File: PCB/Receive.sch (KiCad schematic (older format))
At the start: 9 parts

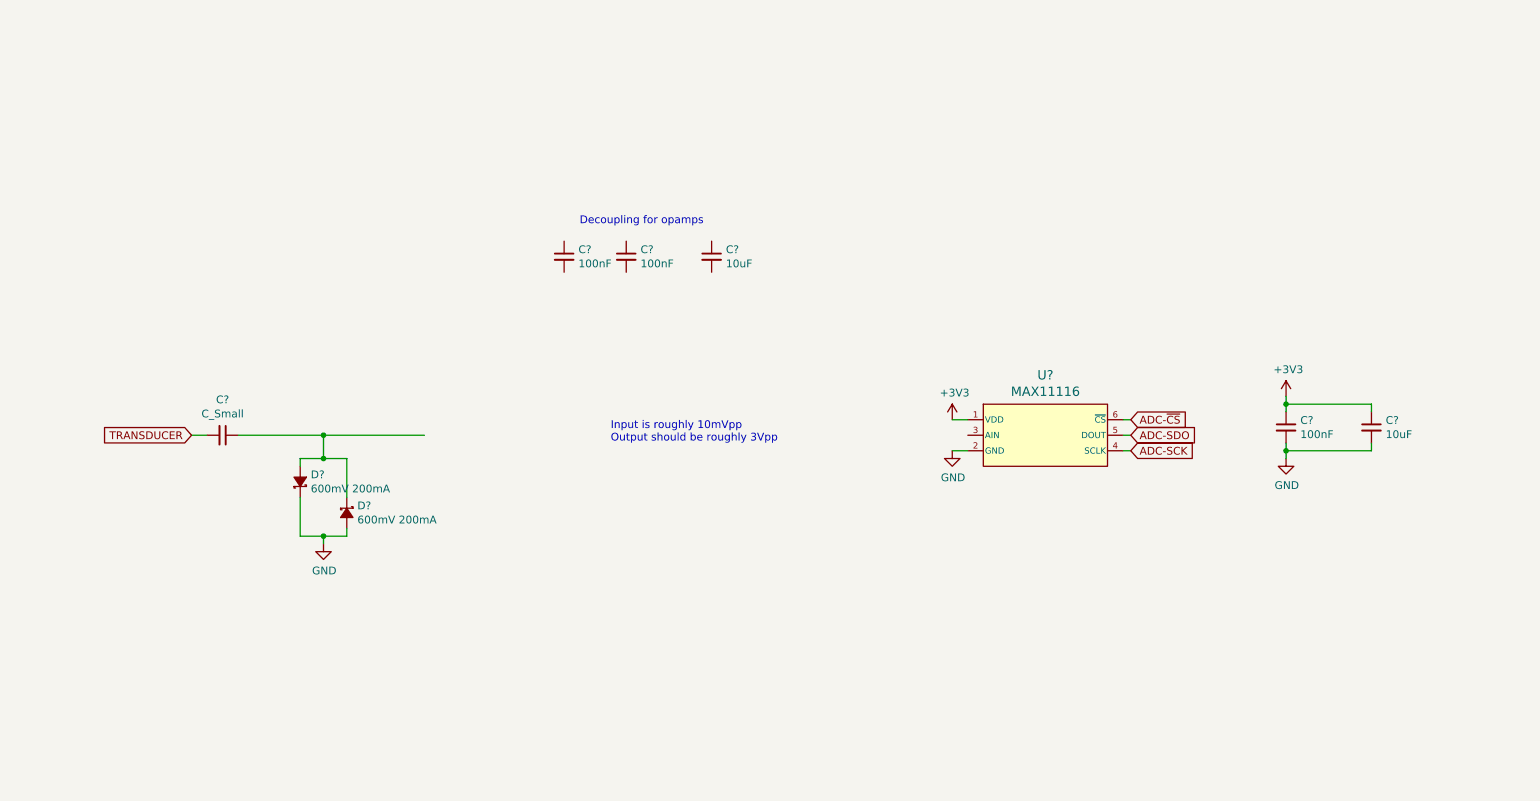
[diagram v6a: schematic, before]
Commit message: Added receive amplification circuit, added opamps for receive to library, added digital potentiometer to library, connected VGA stages to FPGA
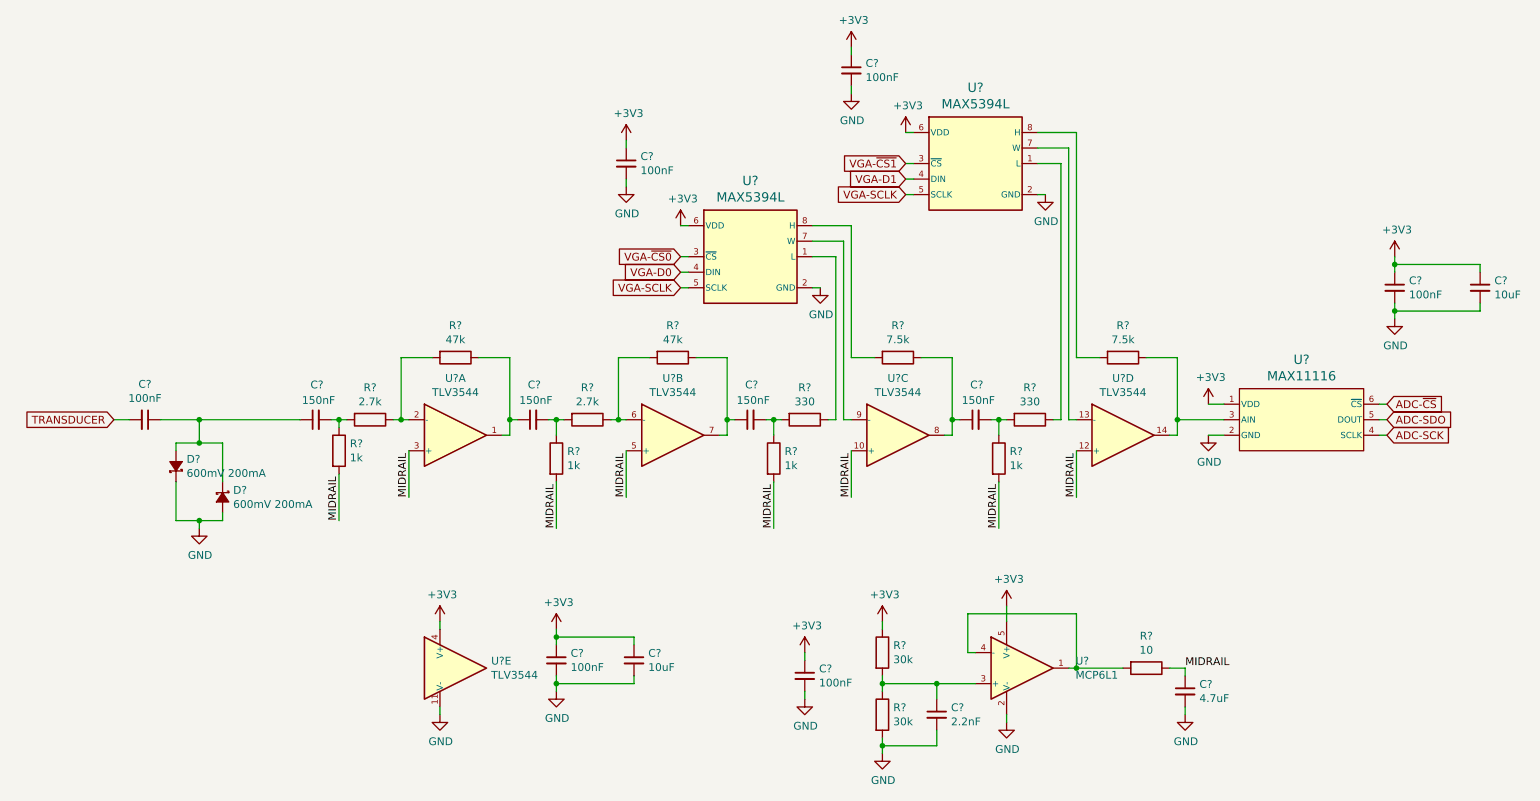
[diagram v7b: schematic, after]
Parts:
- added C? (x4): 150nF, Capacitors_SMD:C_0603_HandSoldering, symbol Device:C_Small
- added C?: 2.2nF, Capacitors_SMD:C_0603_HandSoldering, symbol Device:C_Small
- added C?: 4.7uF, Capacitors_SMD:C_0603_HandSoldering, symbol Device:C_Small
- added C? (x2): 100nF, Capacitors_SMD:C_0603_HandSoldering, symbol Device:C_Small
- added R? (x2): 2.7k, Resistors_SMD:R_0603_HandSoldering, symbol Device:R
- added R? (x2): 47k, Resistors_SMD:R_0603_HandSoldering, symbol Device:R
- added R? (x2): 330, Resistors_SMD:R_0603_HandSoldering, symbol Device:R
- added R? (x2): 7.5k, Resistors_SMD:R_0603_HandSoldering, symbol Device:R
- added R? (x4): 1k, Resistors_SMD:R_0603_HandSoldering, symbol Device:R
- added R? (x2): 30k, Resistors_SMD:R_0603_HandSoldering, symbol Device:R
- added R?: 10, Resistors_SMD:R_0603_HandSoldering, symbol Device:R
- added U?: MCP6L1, Parts:SOT23-5, symbol Parts:MCP6L1
- added U? (x5): TLV3544, Parts:SSOP14, symbol Parts:TLV3544
- added U? (x2): MAX5394L, Parts:TDFN8-PAD, symbol Parts:MAX5394L
- C?: value C_Small -> 100nF; footprint (none) -> Capacitors_SMD:C_1206_HandSoldering
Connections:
- net labels added: MIDRAIL, VGA-D0, VGA-D1, VGA-SCLK, VGA-~CS0, VGA-~CS1
- wire segments 26 -> 139
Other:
- note removed: "Decoupling for opamps"
- note removed: "Input is roughly 10mVpp\nOutput should be roughly 3Vpp"
- moved on the sheet: C?, D?, U?

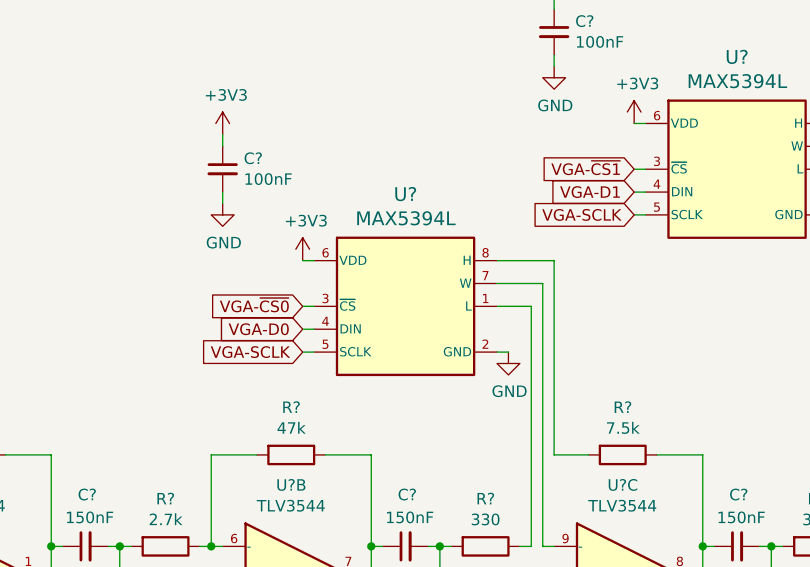
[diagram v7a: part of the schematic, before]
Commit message: Bring additional signals to the connectors sheet for debug access
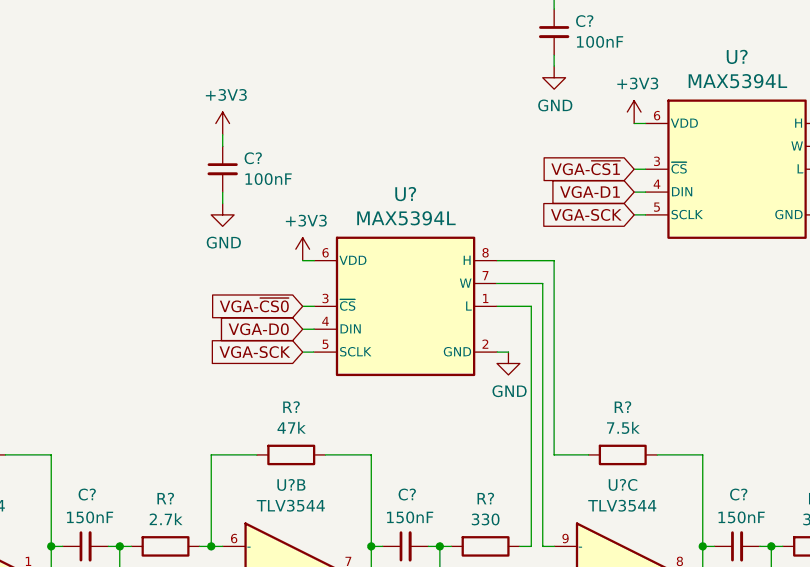
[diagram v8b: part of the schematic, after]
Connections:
- net VGA-SCLK renamed VGA-SCK
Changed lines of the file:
@@
 	6350 1350 6350 1400
 Text GLabel 5250 2900 0    50   Input ~ 0
-VGA-SCLK
+VGA-SCK
 Text GLabel 6700 2300 0    50   Input ~ 0
-VGA-SCLK
+VGA-SCK
 Text GLabel 5250 2800 0    50   Input ~ 0
 VGA-D0
